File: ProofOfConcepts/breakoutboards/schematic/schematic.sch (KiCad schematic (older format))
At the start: 62 parts, among them J1 Conn_01x04_Male, J10 Conn_01x04_Male, J11 Conn_01x04_Male, J2 USB_C_Receptacle_USB2.0, J3 Conn_01x04_Male, J4 Conn_01x04_Male, J5 Conn_01x04_Male, J6 Conn_01x04_Male, J7 Conn_01x04_Male, J8 Conn_01x04_Male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

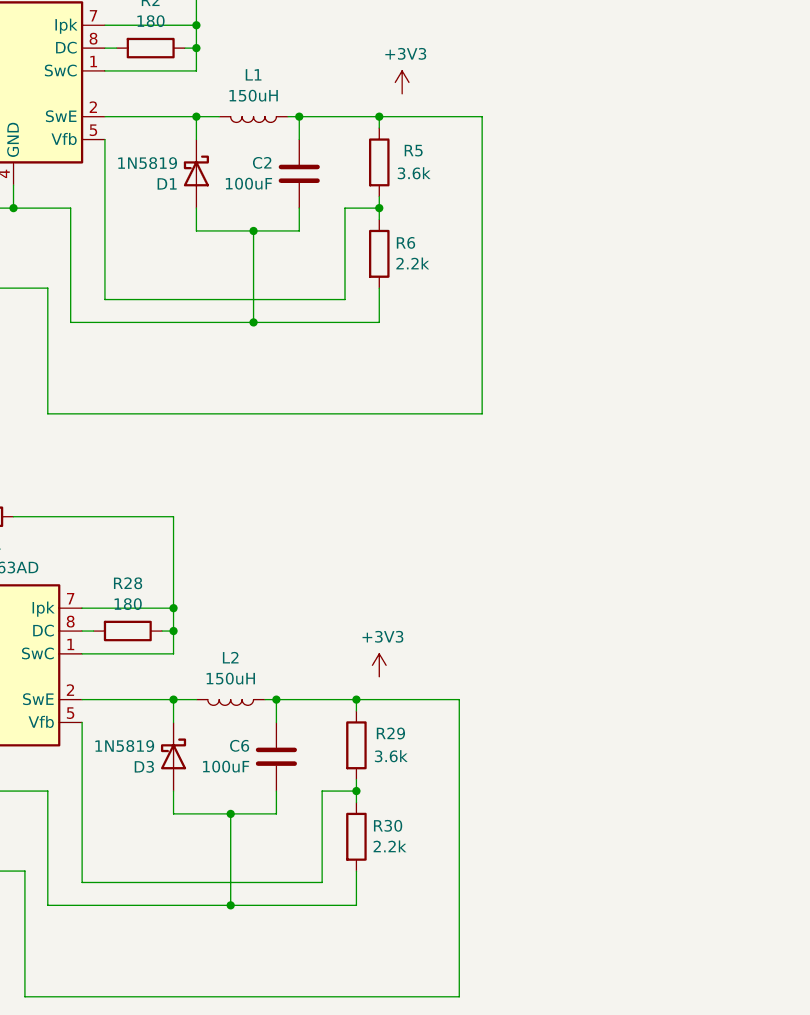
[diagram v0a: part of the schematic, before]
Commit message: updated resistor dividers for more friendly values
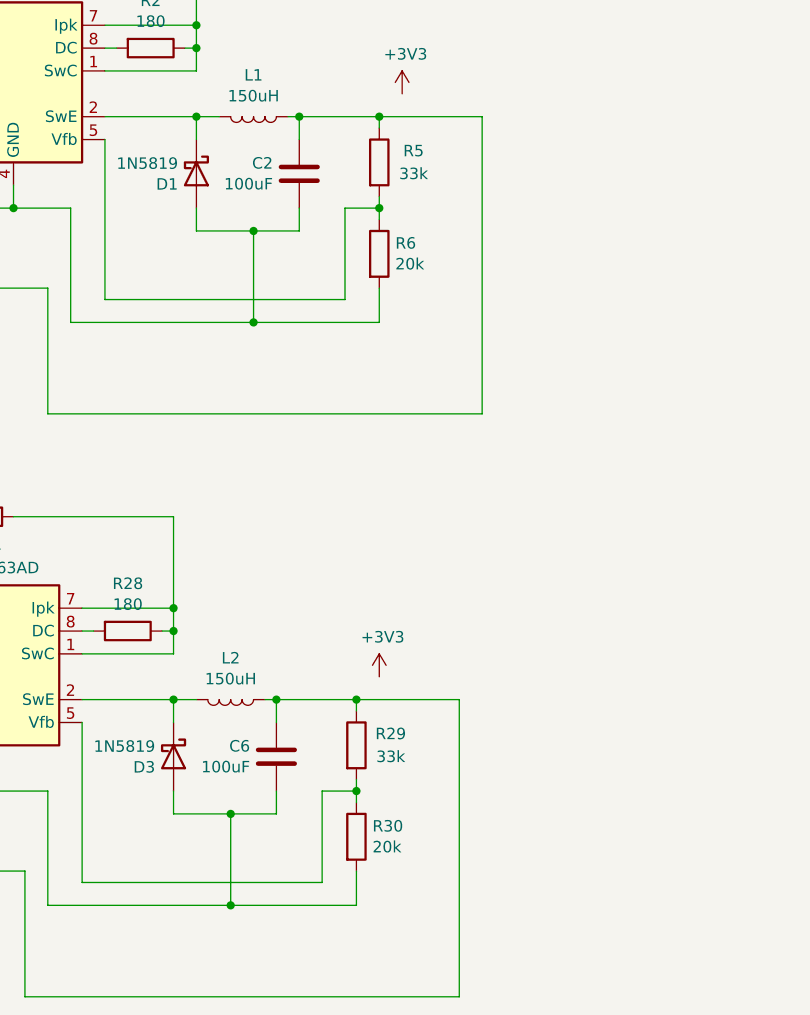
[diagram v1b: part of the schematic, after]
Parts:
- R29, R5: value 3.6k -> 33k
- R30, R6: value 2.2k -> 20k
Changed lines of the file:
@@
 P 5100 7300
 F 0 "R6" H 5170 7346 50  0000 L CNN
-F 1 "2.2k" H 5170 7255 50  0000 L CNN
+F 1 "20k" H 5170 7255 50  0000 L CNN
 F 2 "Resistor_SMD:R_0805_2012Metric_Pad1.20x1.40mm_HandSolder" V 5030 7300 50  0001 C CNN
 F 3 "~" H 5100 7300 50  0001 C CNN
@@
 P 5100 6900
 F 0 "R5" H 5250 6950 50  0000 C CNN
-F 1 "3.6k" H 5250 6850 50  0000 C CNN
+F 1 "33k" H 5250 6850 50  0000 C CNN
 F 2 "Resistor_SMD:R_0805_2012Metric_Pad1.20x1.40mm_HandSolder" V 5030 6900 50  0001 C CNN
 F 3 "~" H 5100 6900 50  0001 C CNN
@@
 P 5000 9850
 F 0 "R30" H 5070 9896 50  0000 L CNN
-F 1 "2.2k" H 5070 9805 50  0000 L CNN
+F 1 "20k" H 5070 9805 50  0000 L CNN
 F 2 "Resistor_SMD:R_0805_2012Metric_Pad1.20x1.40mm_HandSolder" V 4930 9850 50  0001 C CNN
 F 3 "~" H 5000 9850 50  0001 C CNN
@@
 P 5000 9450
 F 0 "R29" H 5150 9500 50  0000 C CNN
-F 1 "3.6k" H 5150 9400 50  0000 C CNN
+F 1 "33k" H 5150 9400 50  0000 C CNN
 F 2 "Resistor_SMD:R_0805_2012Metric_Pad1.20x1.40mm_HandSolder" V 4930 9450 50  0001 C CNN
 F 3 "~" H 5000 9450 50  0001 C CNN
